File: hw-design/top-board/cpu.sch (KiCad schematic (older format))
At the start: 12 parts

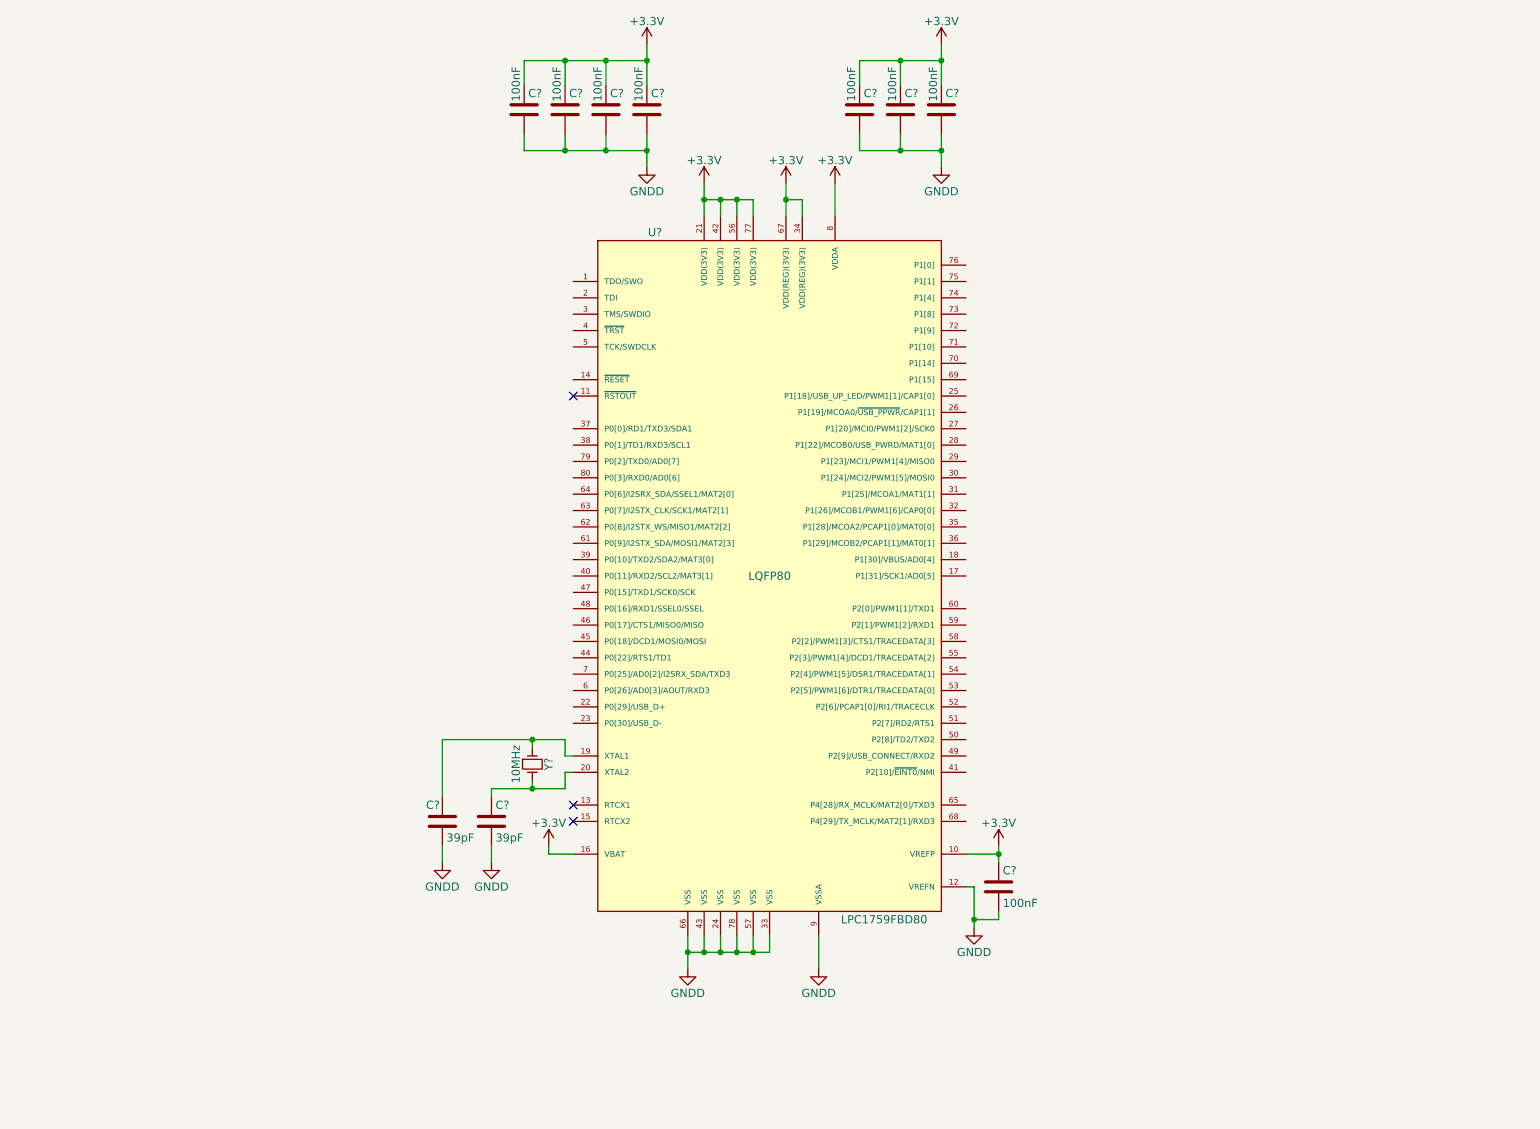
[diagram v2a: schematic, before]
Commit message: sch,top-board: adding uC signals (wip)
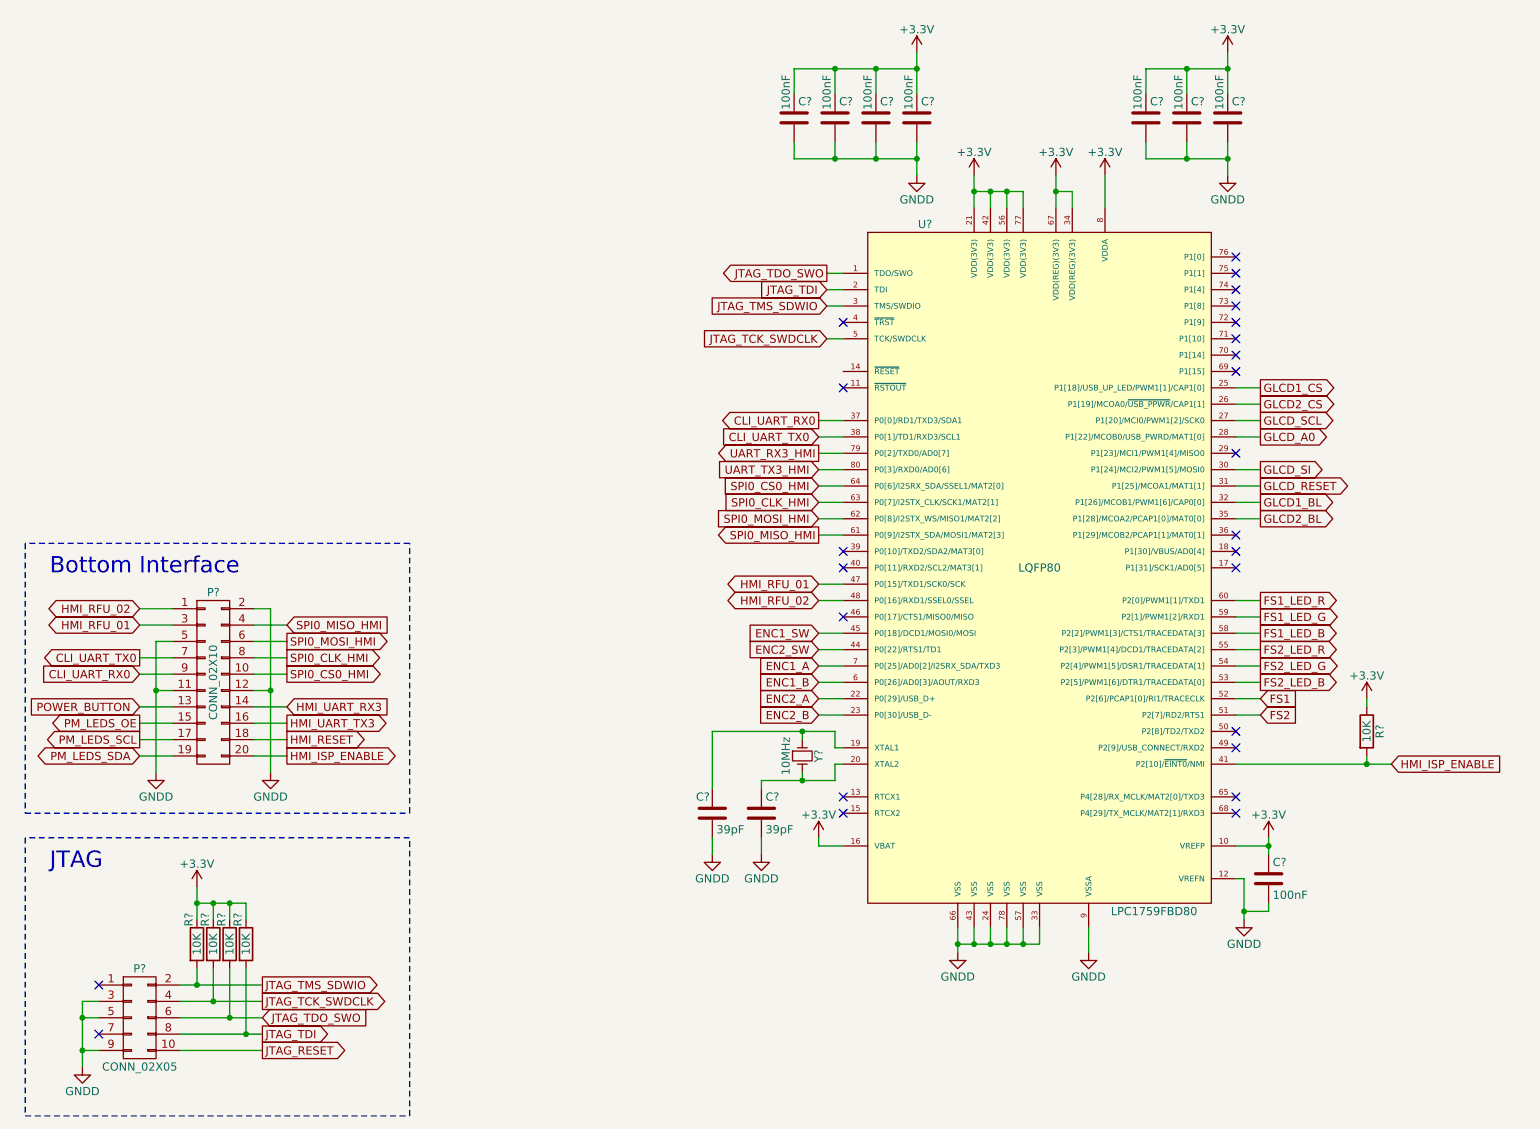
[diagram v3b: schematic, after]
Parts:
- added P?: CONN_02X10, symbol CONN_02X10
- added P?: CONN_02X05, symbol CONN_02X05
- added R? (x5): 10K, symbol R
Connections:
- net +3V3: now also R?.1, R?.1, R?.1, R?.1, R?.1
- net GNDD: now also P?.11 (P11), P?.12 (P12), P?.2 (P2), P?.3 (P3), P?.5 (P5), P?.5 (P5), P?.9 (P9)
- net JTAG_TDO_SWO: now reaches U?.1 (TDO/SWO)
- net JTAG_TDO_SWO: now also P?.6 (P6), R?.2
- net JTAG_TDI: now reaches U?.2 (TDI)
- net JTAG_TDI: now also P?.8 (P8), R?.2
- net ENC2_A: now reaches U?.22 (P0[29]/USB_D+)
- net ENC2_B: now reaches U?.23 (P0[30]/USB_D-)
- net GLCD1_CS: now reaches U?.25 (P1[18]/USB_UP_LED/PWM1[1]/CAP1[0])
- net GLCD2_CS: now reaches U?.26 (P1[19]/MCOA0/~USB_PPWR~/CAP1[1])
- net GLCD_SCL: now reaches U?.27 (P1[20]/MCI0/PWM1[2]/SCK0)
- net GLCD_A0: now reaches U?.28 (P1[22]/MCOB0/USB_PWRD/MAT1[0])
- net JTAG_TMS_SDWIO: now reaches U?.3 (TMS/SWDIO)
- net JTAG_TMS_SDWIO: now also P?.2 (P2), R?.2
- net GLCD_SI: now reaches U?.30 (P1[24]/MCI2/PWM1[5]/MOSI0)
- net GLCD_RESET: now reaches U?.31 (P1[25]/MCOA1/MAT1[1])
- net GLCD1_BL: now reaches U?.32 (P1[26]/MCOB1/PWM1[6]/CAP0[0])
- net GLCD2_BL: now reaches U?.35 (P1[28]/MCOA2/PCAP1[0]/MAT0[0])
- net CLI_UART_RX0: now reaches U?.37 (P0[0]/RD1/TXD3/SDA1)
- net CLI_UART_RX0: now also P?.9 (P9)
- net CLI_UART_TX0: now reaches U?.38 (P0[1]/TD1/RXD3/SCL1)
- net CLI_UART_TX0: now also P?.7 (P7)
- net HMI_ISP_ENABLE: now reaches U?.41 (P2[10]/~EINT0~/NMI)
- net HMI_ISP_ENABLE: now also P?.20 (P20), R?.2
- net ENC2_SW: now reaches U?.44 (P0[22]/RTS1/TD1)
- net ENC1_SW: now reaches U?.45 (P0[18]/DCD1/MOSI0/MOSI)
- net HMI_RFU_01: now reaches U?.47 (P0[15]/TXD1/SCK0/SCK)
- net HMI_RFU_01: now also P?.3 (P3)
- net HMI_RFU_02: now reaches U?.48 (P0[16]/RXD1/SSEL0/SSEL)
- net HMI_RFU_02: now also P?.1 (P1)
- net JTAG_TCK_SWDCLK: now reaches U?.5 (TCK/SWDCLK)
- net JTAG_TCK_SWDCLK: now also P?.4 (P4), R?.2
- net FS2: now reaches U?.51 (P2[7]/RD2/RTS1)
- net FS1: now reaches U?.52 (P2[6]/PCAP1[0]/RI1/TRACECLK)
- net FS2_LED_B: now reaches U?.53 (P2[5]/PWM1[6]/DTR1/TRACEDATA[0])
- net FS2_LED_G: now reaches U?.54 (P2[4]/PWM1[5]/DSR1/TRACEDATA[1])
- net FS2_LED_R: now reaches U?.55 (P2[3]/PWM1[4]/DCD1/TRACEDATA[2])
- net FS1_LED_B: now reaches U?.58 (P2[2]/PWM1[3]/CTS1/TRACEDATA[3])
- net FS1_LED_G: now reaches U?.59 (P2[1]/PWM1[2]/RXD1)
- net ENC1_B: now reaches U?.6 (P0[26]/AD0[3]/AOUT/RXD3)
- net FS1_LED_R: now reaches U?.60 (P2[0]/PWM1[1]/TXD1)
- net SPI0_MISO_HMI: now reaches U?.61 (P0[9]/I2STX_SDA/MOSI1/MAT2[3])
- net SPI0_MISO_HMI: now also P?.4 (P4)
- net SPI0_MOSI_HMI: now reaches U?.62 (P0[8]/I2STX_WS/MISO1/MAT2[2])
- net SPI0_MOSI_HMI: now also P?.6 (P6)
- net SPI0_CLK_HMI: now reaches U?.63 (P0[7]/I2STX_CLK/SCK1/MAT2[1])
- net SPI0_CLK_HMI: now also P?.8 (P8)
- net SPI0_CS0_HMI: now reaches U?.64 (P0[6]/I2SRX_SDA/SSEL1/MAT2[0])
- net SPI0_CS0_HMI: now also P?.10 (P10)
- net ENC1_A: now reaches U?.7 (P0[25]/AD0[2]/I2SRX_SDA/TXD3)
- net UART_RX3_HMI: now reaches U?.79 (P0[2]/TXD0/AD0[7])
- net UART_TX3_HMI: now reaches U?.80 (P0[3]/RXD0/AD0[6])
- new net HMI_RESET: P?.18 (P18)
- new net HMI_UART_RX3: P?.14 (P14)
- new net HMI_UART_TX3: P?.16 (P16)
- new net JTAG_RESET: P?.10 (P10)
- new net PM_LEDS_OE: P?.15 (P15)
- new net PM_LEDS_SCL: P?.17 (P17)
- new net PM_LEDS_SDA: P?.19 (P19)
- new net POWER_BUTTON: P?.13 (P13)
- no-connect marks 3 -> 25
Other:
- note added: "Bottom Interface"
- note added: "JTAG"
- moved on the sheet: C?, U?, Y?

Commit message: sch,top-board: added uC signals
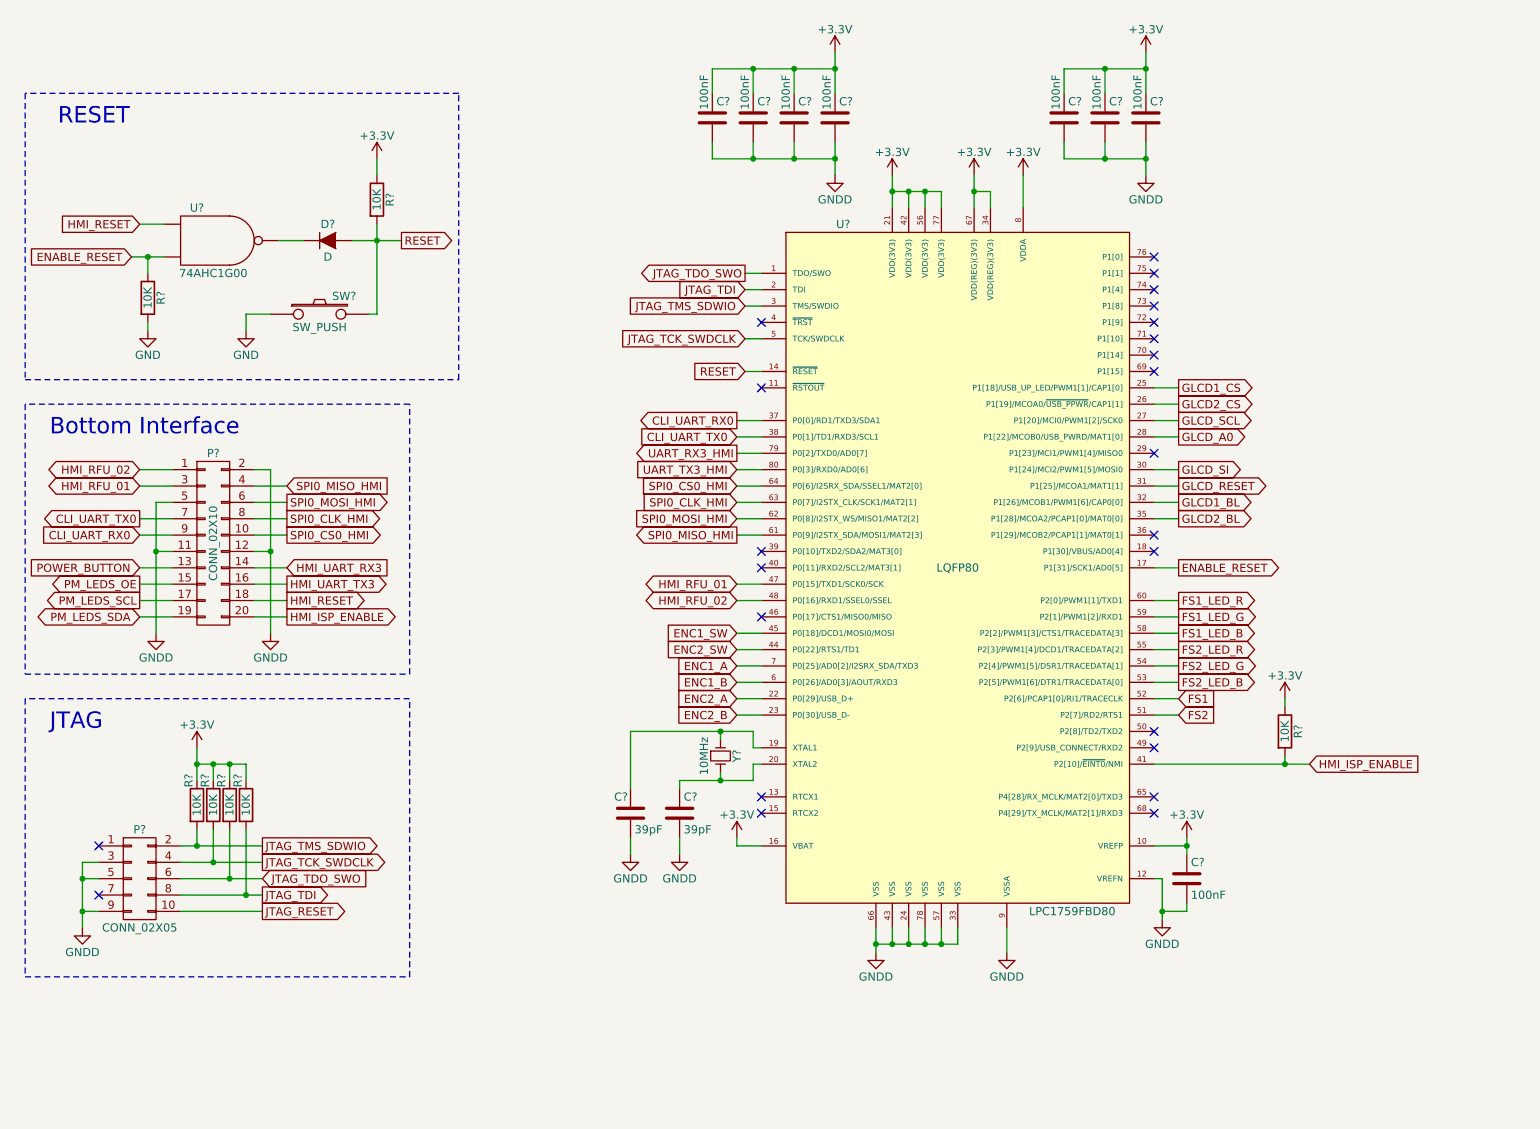
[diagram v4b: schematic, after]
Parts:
- added D?: D, symbol D
- added R? (x2): 10K, symbol R
- added SW?: SW_PUSH, symbol SW_PUSH
- added U?: 74AHC1G00, symbol 74AHC1G00
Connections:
- net +3V3: now also R?.1
- net HMI_RESET: now also U?.1
- net RESET: now reaches U?.14 (~RESET~)
- net RESET: now also D?.2 (A), R?.2, SW?.2
- net ENABLE_RESET: now reaches U?.17 (P1[31]/SCK1/AD0[5])
- net ENABLE_RESET: now also R?.1, U?.2
- new net: D?.1 (K), U?.4
- new net GND: R?.2, SW?.1, U?.3 (GND)
- new net VCC: U?.5 (VCC)
- no-connect marks 25 -> 24
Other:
- note added: "RESET"
- moved on the sheet: C?, P?, R?, U?, Y?

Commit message: sch,top-board: annotation done
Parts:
- added D2: D, symbol D
- added P6: CONN_02X04, symbol CONN_02X04
- gave numbers to parts that had none: 24
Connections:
- net JTAG_TCK_SWDCLK: now also P6.4 (P4)
- net JTAG_TDI: now also P6.8 (P8)
- net JTAG_TDO_SWO: now also P6.6 (P6)
- net JTAG_TMS_SDWIO: now also P6.2 (P2)
- net RESET: now also D2.2 (A)
- net SPI0_CLK_HMI: now also P6.3 (P3)
- net SPI0_CS0_HMI: now also P6.1 (P1)
- net SPI0_MISO_HMI: now also P6.5 (P5)
- net SPI0_MOSI_HMI: now also P6.7 (P7)
- net JTAG_RESET: no longer names the net of P5.10 (P10)
- net JTAG_RESET: now also D2.1 (K)
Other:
- moved on the sheet: D1, P4, P5, R3, R4, R6, R7, R8, R9, SW1, U2

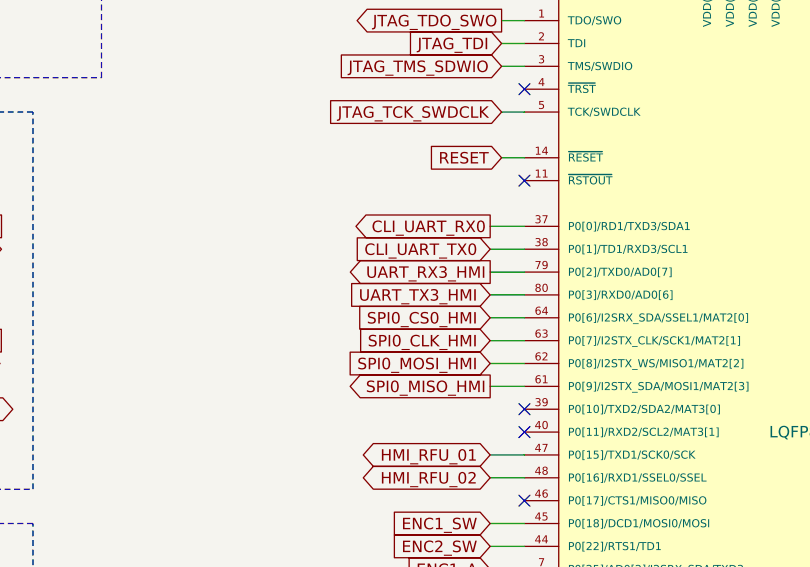
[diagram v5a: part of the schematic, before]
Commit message: sch,top-board: fix signals names and unconnected wire
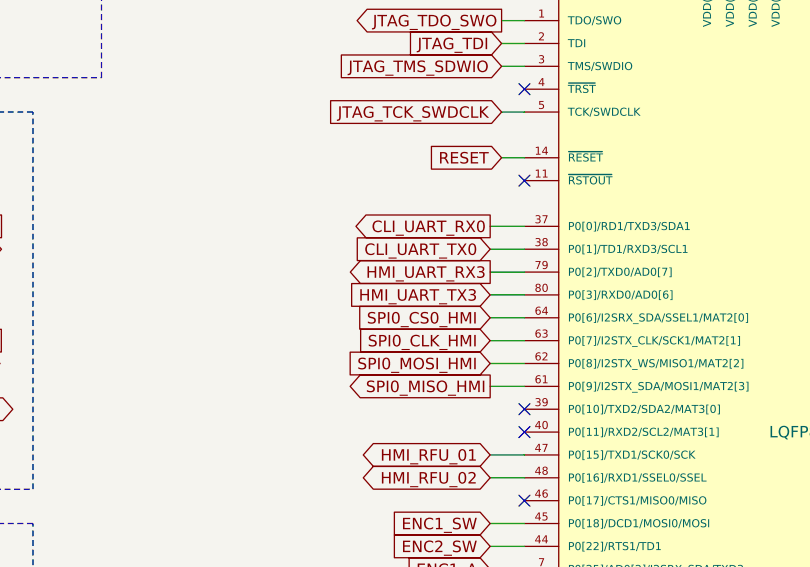
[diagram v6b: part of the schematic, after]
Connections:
- net UART_RX3_HMI is gone; now on net HMI_UART_RX3: U3.79 (P0[2]/TXD0/AD0[7])
- net UART_TX3_HMI is gone; now on net HMI_UART_TX3: U3.80 (P0[3]/RXD0/AD0[6])
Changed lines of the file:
@@
 PM_LEDS_OE
 Text GLabel 5350 3250 0    50   Output ~ 0
-UART_RX3_HMI
+HMI_UART_RX3
 Text GLabel 5350 3350 0    50   Input ~ 0
-UART_TX3_HMI
+HMI_UART_TX3
 Text GLabel 8850 5150 2    50   Input ~ 0
 HMI_ISP_ENABLE

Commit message: sch,top-board: DRC passing
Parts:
- renumbered R8 to R10, R9 to R11, R3 to R5, R4 to R6, R5 to R7, R6 to R8, R7 to R9
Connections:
- net GND: no longer R6.2, SW1.1
- net GNDD: now also R6.2, SW1.1
- net POWER_BUTTON: now also U3.18 (P1[30]/VBUS/AD0[4])
- no-connect marks 24 -> 23

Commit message: sch,top-board: BOM added
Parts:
- C27, C28, C29, C30, C31, C32, C33, C36: MPN (none) -> C1608X7R1E104K080AA
- C34, C35: MPN (none) -> GRM1555C1H390JA01D
- D1, D2: MPN (none) -> 1N4148WX-TP
- P4: MPN (none) -> SBH11-PBPC-D10-ST-BK
- R10, R11, R5, R6, R7, R8, R9: MPN (none) -> RMCF0603JT10K0
- SW1: MPN (none) -> FSMSM
- U2: MPN (none) -> 74AHC1G00SE-7
- U3: MPN (none) -> LPC1759FBD80,551
